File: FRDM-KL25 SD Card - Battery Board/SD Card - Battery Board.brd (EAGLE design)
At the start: 81.3 x 53.3 mm, 70 parts, among them J10 SSW-103-02-S-S, J11 SSW-102-02-S-S, J12 SSW-103-02-S-S, J13 SSW-103-02-S-S, J14 SSW-103-02-S-S, J15 SSW-103-02-S-S, J16 SSW-103-02-S-S, J17 SSW-103-02-S-S, J18 SSW-103-02-S-S, J19 501568-0207-V2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

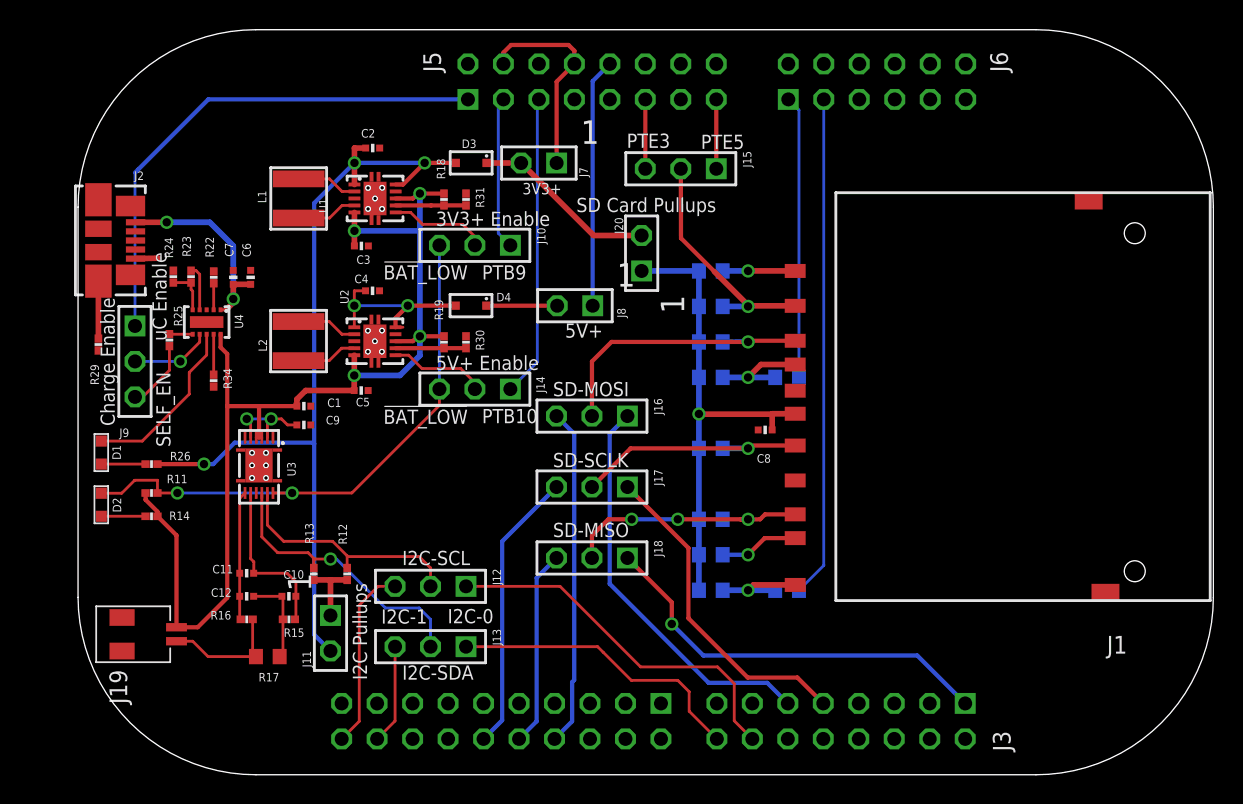
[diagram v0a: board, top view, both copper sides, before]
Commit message: FRDM-KL25Z-I: Some routing have been slighty shifted to give a cleaner look and better electrical flow
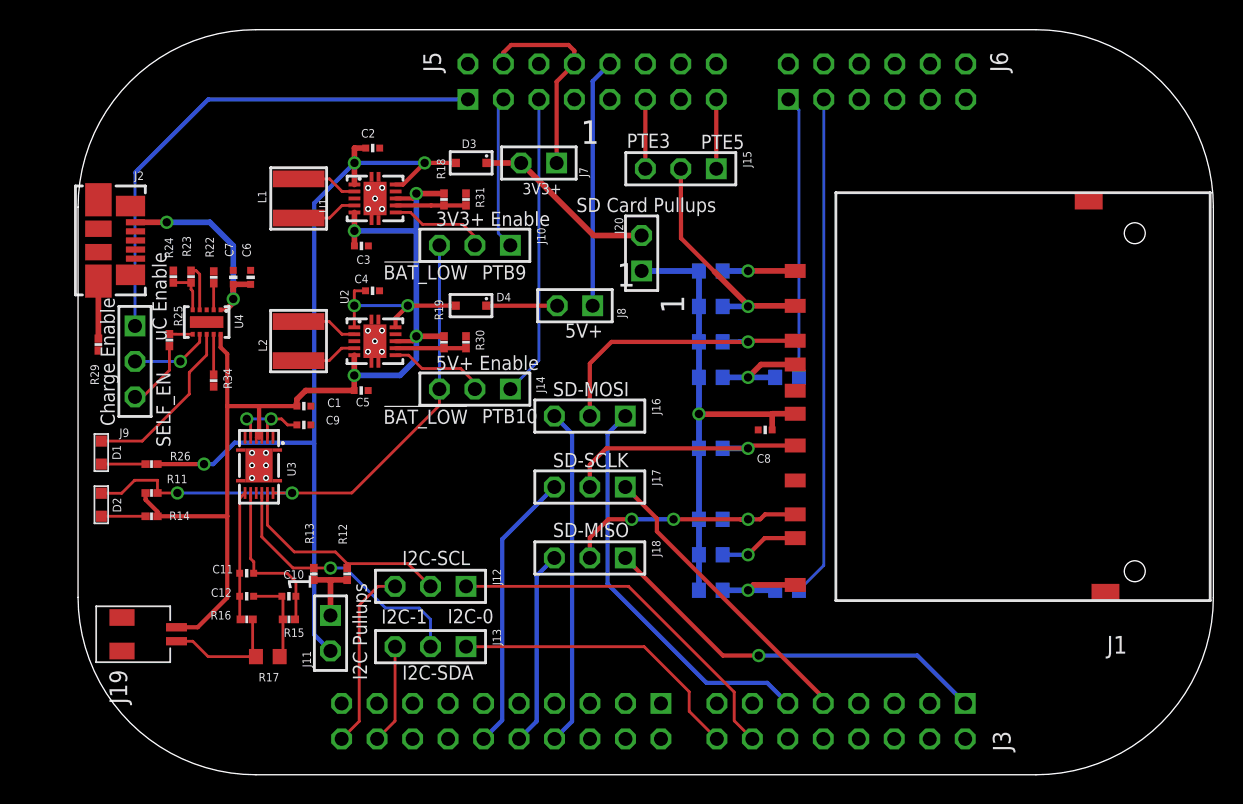
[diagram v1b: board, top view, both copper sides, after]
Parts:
- moved J16 0.15 mm to (21.7, 22.9)
- moved J17 0.15 mm to (21.7, 17.8)
- moved J18 0.15 mm to (21.7, 12.7)
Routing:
- net PACK+: track 80.3 -> 76.6 mm
- net SPI-SCLK-SD-B: track 23.4 -> 21.4 mm
- net GND: track 8.15 -> 6.51 mm
- net SCL: track 17.4 -> 16.1 mm
- net N$30: track 17.6 -> 18.7 mm
- net SPI-MISO-SD-B: track 29.4 -> 28.6 mm
- net SDA: track 20.3 -> 19.6 mm
- net N$20: track 13.1 -> 12.6 mm

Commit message: FRDM-KL25Z-I: Fixing a critical issue with power to the SD Card, when pullups are disabled so was the SD Card this has been partialy fixed but there is still a missing link from 3V3-SD to the SD Card. Also in need is the purpetual power to the Card Detect and Write Protect pins, this also needs to be connected to 3V3-SD
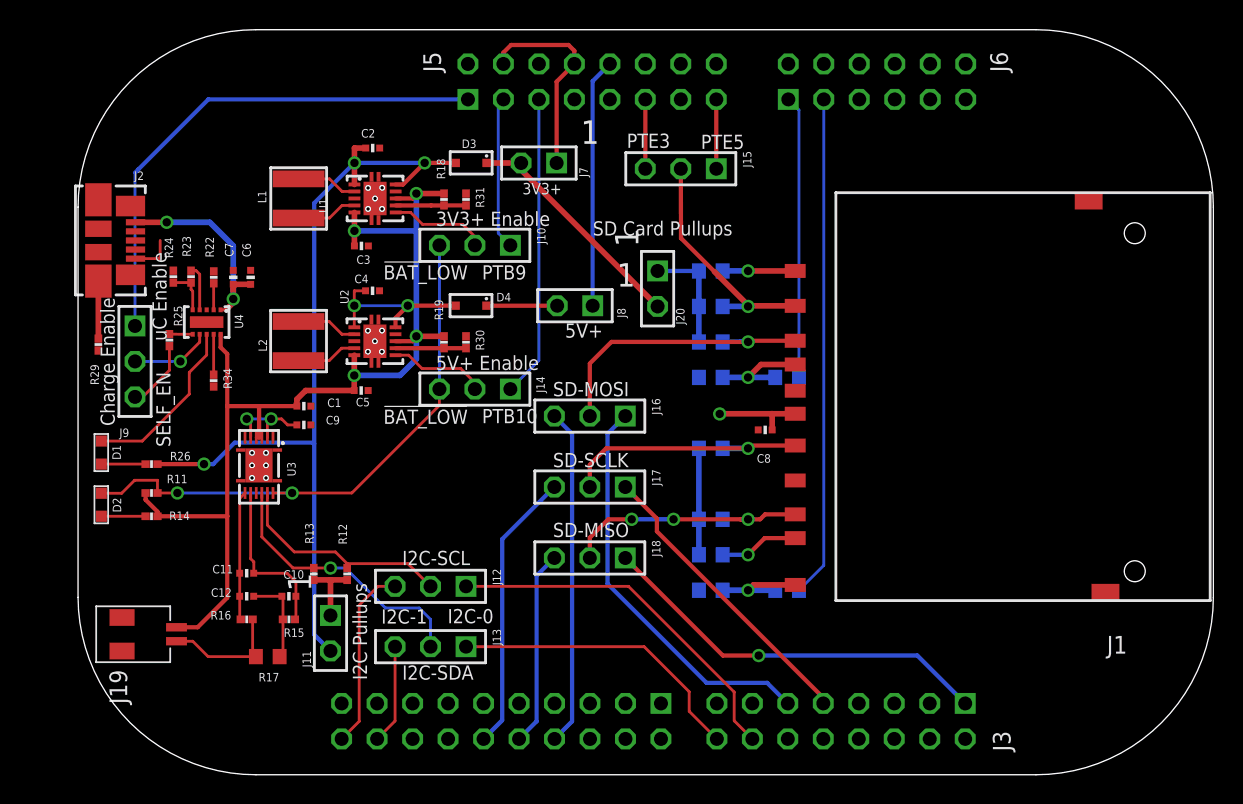
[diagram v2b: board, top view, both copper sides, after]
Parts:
- moved J20 2.79 mm to (26.5, 32.0), turned to 270 degrees
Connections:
- removed net N$17: D3.P$1, J20.2, J7.2
- new net +3V3-SD-PULLUP: J20.1, R1.2, R2.2, R3.2, R4.2, R5.2, R6.2
- net +3V3-SD: now also D3.P$1, J20.2, J7.2; no longer J20.1, R1.2, R2.2, R3.2, R4.2, R5.2, R6.2
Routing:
- net +3V3-SD-PULLUP: track 0.00 -> 15.7 mm
- net N$17: track 13.3 -> 0.00 mm
- net +3V3-SD: track 35.1 -> 23.3 mm
- net GND: track 6.51 -> 9.57 mm
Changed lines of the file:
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@@
 <text x="16.8656" y="38.735" size="0.8128" layer="21" ratio="5">3V3+</text>
 <text x="19.9136" y="28.4734" size="1.016" layer="21" ratio="5">5V+</text>
-<text x="20.7264" y="37.465" size="1.016" layer="21" ratio="5">SD Card Pullups</text>
+<text x="21.8948" y="35.7886" size="1.016" layer="21" ratio="5">SD Card Pullups</text>
 <text x="29.6418" y="41.9862" size="1.016" layer="21" ratio="5">PTE5</text>
 <text x="24.3332" y="42.0624" size="1.016" layer="21" ratio="5">PTE3</text>
@@
 <attribute name="VALUE" x="-13.97" y="4.699" size="1.27" layer="27" rot="R270"/>
 </element>
-<element name="J20" library="Kas-Connectors" package="SSW-102-02-S-S" value="SSW-102-02-S-S" x="25.4" y="34.5186" smashed="yes" rot="R90">
-<attribute name="OC_NEWARK" value="11P9351" x="25.4" y="34.5186" size="1.778" layer="27" rot="R90" display="off"/>
-<attribute name="MPN" value="SSW-102-02-S-S" x="25.4" y="34.5186" size="1.778" layer="27" rot="R90" display="off"/>
-<attribute name="MF" value="" x="25.4" y="34.5186" size="1.778" layer="27" rot="R90" display="off"/>
-<attribute name="OC_FARNELL" value="unknown" x="25.4" y="34.5186" size="1.778" layer="27" rot="R90" display="off"/>
-<attribute name="NAME" x="23.4696" y="37.084" size="0.6096" layer="25" rot="R270"/>
-<attribute name="VALUE" x="26.67" y="38.9636" size="1.27" layer="27" rot="R180"/>
+<element name="J20" library="Kas-Connectors" package="SSW-102-02-S-S" value="SSW-102-02-S-S" x="26.543" y="31.9786" smashed="yes" rot="R270">
+<attribute name="OC_NEWARK" value="11P9351" x="26.543" y="31.9786" size="1.778" layer="27" rot="R270" display="off"/>
+<attribute name="MPN" value="SSW-102-02-S-S" x="26.543" y="31.9786" size="1.778" layer="27" rot="R270" display="off"/>
+<attribute name="MF" value="" x="26.543" y="31.9786" size="1.778" layer="27" rot="R270" display="off"/>
+<attribute name="OC_FARNELL" value="unknown" x="26.543" y="31.9786" size="1.778" layer="27" rot="R270" display="off"/>
+<attribute name="NAME" x="28.4734" y="29.4132" size="0.6096" layer="25" rot="R90"/>
+<attribute name="VALUE" x="25.273" y="27.5336" size="1.27" layer="27"/>
 </element>
 </elements>
 <signals>
-<signal name="GND">
+<signal name="GND" airwireshidden="yes">
 <contactref element="U3" pad="P$1"/>
 <contactref element="U3" pad="P$6"/>
@@
 <wire x1="-0.27768125" y1="8.3058" x2="-0.27768125" y2="5.8751" width="0.2032" layer="1"/>
 <wire x1="-0.27768125" y1="5.8751" x2="-0.51398125" y2="5.6388" width="0.2032" layer="1"/>
+<wire x1="-10.8331" y1="34.133" x2="-9.0678" y2="34.133" width="0.2032" layer="1"/>
+<wire x1="-9.0678" y1="34.133" x2="-9.0678" y2="35.433" width="0.2032" layer="1"/>
 <wire x1="25.66543125" y1="48.071278125" x2="28.20543125" y2="48.071278125" width="0" layer="19" extent="1-1"/>
 <wire x1="12.827" y1="38.79121875" x2="25.66543125" y2="48.071278125" width="0" layer="19" extent="1-1"/>
@@
 <wire x1="-2.5908" y1="33.2914" x2="-3.8354" y2="33.2914" width="0" layer="19" extent="1-1"/>
 <wire x1="-8.128" y1="33.2672" x2="-5.2324" y2="33.2164" width="0" layer="19" extent="1-1"/>
-<wire x1="-10.8331" y1="34.133" x2="-8.128" y2="33.2672" width="0" layer="19" extent="1-1"/>
+<wire x1="-9.0678" y1="34.133" x2="-8.128" y2="33.2672" width="0" layer="19" extent="1-1"/>
 <wire x1="12.827" y1="28.5708" x2="7.7802" y2="28.7186" width="0" layer="19" extent="1-1"/>
 <wire x1="-13.4931" y1="27.5562" x2="-10.8331" y2="34.133" width="0" layer="19" extent="1-1"/>
@@
 <contactref element="J1" pad="P$4"/>
 <contactref element="C8" pad="1"/>
+<wire x1="36.396" y1="23.0256" x2="34.746" y2="23.0256" width="0.4064" layer="1"/>
+<wire x1="34.746" y1="21.8692" x2="34.746" y2="23.0256" width="0.4064" layer="1"/>
+<via x="30.988" y="23.0124" extent="1-16" drill="0.6"/>
+<contactref element="D3" pad="P$1"/>
+<contactref element="J7" pad="2"/>
+<contactref element="J20" pad="2"/>
+<wire x1="14.294759375" y1="40.985109375" x2="14.30205" y2="40.97781875" width="0.2032" layer="1"/>
+<wire x1="14.30205" y1="40.97781875" x2="16.774159375" y2="40.97781875" width="0.4064" layer="1"/>
+<wire x1="26.543" y1="30.7086" x2="16.774159375" y2="40.477440625" width="0.4064" layer="1"/>
+<wire x1="16.774159375" y1="40.477440625" x2="16.774159375" y2="40.97781875" width="0.4064" layer="1"/>
+<wire x1="31.0012" y1="23.0256" x2="34.746" y2="23.0256" width="0.4064" layer="1"/>
+<contactref element="R7" pad="2"/>
+<contactref element="R8" pad="2"/>
+<wire x1="31.0012" y1="23.0256" x2="30.988" y2="23.0124" width="0" layer="19" extent="1-1"/>
+<wire x1="29.503" y1="25.6286" x2="30.988" y2="23.0124" width="0" layer="19" extent="16-16"/>
+<wire x1="26.543" y1="30.7086" x2="29.503" y2="25.6286" width="0" layer="19" extent="16-16"/>
+<wire x1="29.503" y1="10.3886" x2="34.746" y2="21.8692" width="0" layer="19" extent="1-16"/>
+</signal>
+<signal name="+3V3-SD-PULLUP">
 <contactref element="R1" pad="2"/>
-<contactref element="R8" pad="2"/>
 <contactref element="R2" pad="2"/>
 <contactref element="R3" pad="2"/>
@@
 <contactref element="R5" pad="2"/>
 <contactref element="R6" pad="2"/>
-<contactref element="R7" pad="2"/>
 <wire x1="29.503" y1="28.1686" x2="29.503" y2="30.7086" width="0.4064" layer="16"/>
 <wire x1="29.503" y1="30.7086" x2="29.503" y2="33.2486" width="0.4064" layer="16"/>
 <wire x1="29.503" y1="20.5486" x2="29.503" y2="15.4686" width="0.4064" layer="16"/>
 <wire x1="29.503" y1="12.9286" x2="29.503" y2="15.4686" width="0.4064" layer="16"/>
-<wire x1="29.503" y1="12.9286" x2="29.503" y2="10.3886" width="0.4064" layer="16"/>
-<wire x1="36.396" y1="23.0256" x2="34.746" y2="23.0256" width="0.4064" layer="1"/>
-<wire x1="34.746" y1="21.8692" x2="34.746" y2="22.9948375" width="0.4064" layer="1"/>
 <contactref element="J20" pad="1"/>
-<wire x1="34.746" y1="22.9948375" x2="34.746" y2="23.0256" width="0.4064" layer="1"/>
-<wire x1="34.746" y1="22.9948375" x2="29.4561625" y2="22.9948375" width="0.4064" layer="1"/>
-<wire x1="29.4561625" y1="22.9948375" x2="29.503" y2="23.0124" width="0.4064" layer="1"/>
-<via x="29.503" y="23.0124" extent="1-16" drill="0.6"/>
-<wire x1="29.503" y1="23.0124" x2="29.503" y2="28.1686" width="0.4064" layer="16"/>
-<wire x1="29.503" y1="20.5486" x2="29.503" y2="23.0124" width="0.4064" layer="16"/>
-<wire x1="25.4" y1="33.2486" x2="29.503" y2="33.2486" width="0.4064" layer="16"/>
-<wire x1="29.503" y1="28.1686" x2="29.503" y2="25.6286" width="0" layer="19" extent="16-16"/>
-</signal>
-<signal name="N$17">
-<contactref element="D3" pad="P$1"/>
-<contactref element="J7" pad="2"/>
-<contactref element="J20" pad="2"/>
-<wire x1="14.294759375" y1="40.985109375" x2="14.30205" y2="40.97781875" width="0.2032" layer="1"/>
-<wire x1="14.30205" y1="40.97781875" x2="16.774159375" y2="40.97781875" width="0.4064" layer="1"/>
-<wire x1="16.774159375" y1="40.97781875" x2="21.963378125" y2="35.7886" width="0.4064" layer="1"/>
-<wire x1="21.963378125" y1="35.7886" x2="25.4" y2="35.7886" width="0.4064" layer="1"/>
+<wire x1="26.543" y1="33.2486" x2="29.503" y2="33.2486" width="0.3048" layer="16"/>
+<wire x1="29.503" y1="20.5486" x2="29.503" y2="28.1686" width="0" layer="19" extent="16-16"/>
 </signal>
 </signals>

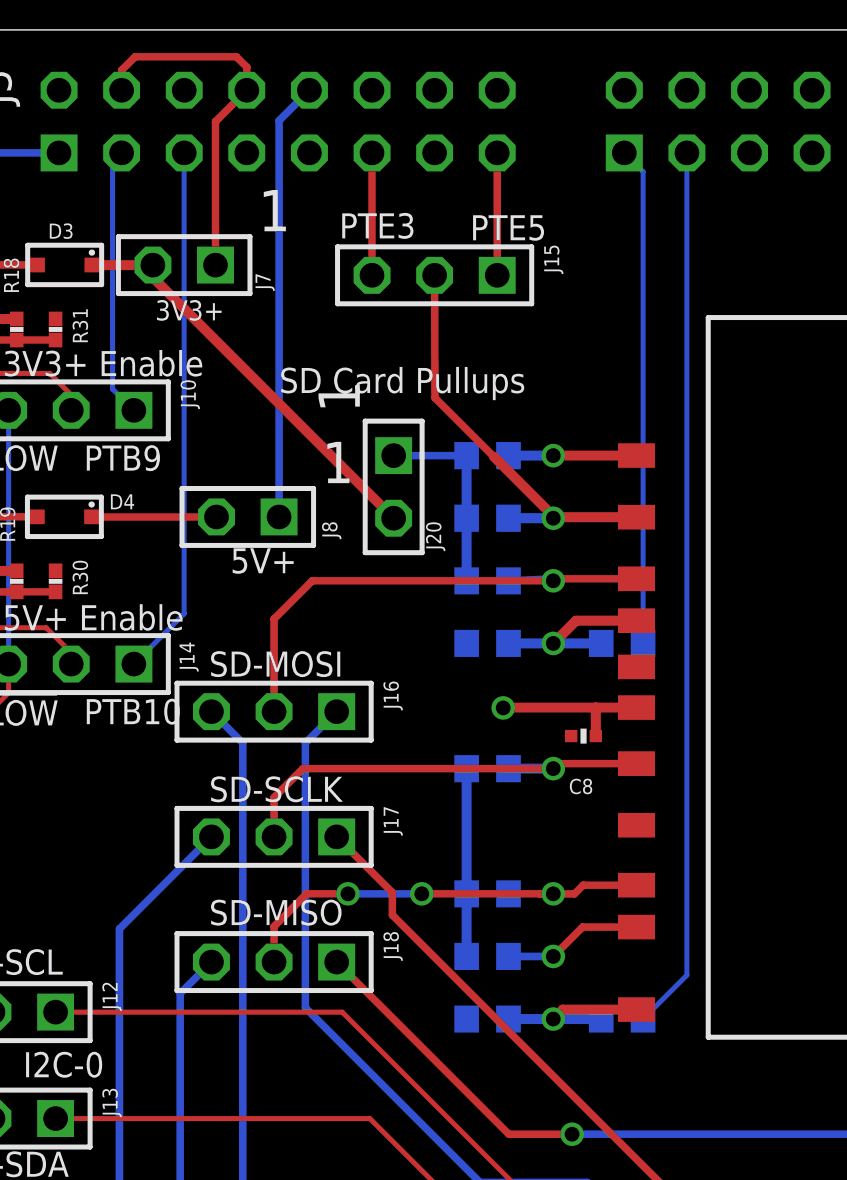
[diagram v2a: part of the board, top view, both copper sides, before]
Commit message: FRDM-KL25Z-I: SD Card power issue is resolved, connections have been rerouted to allow for the SD Card to always be powerd as well for the card detect and write protect to be always powerd.
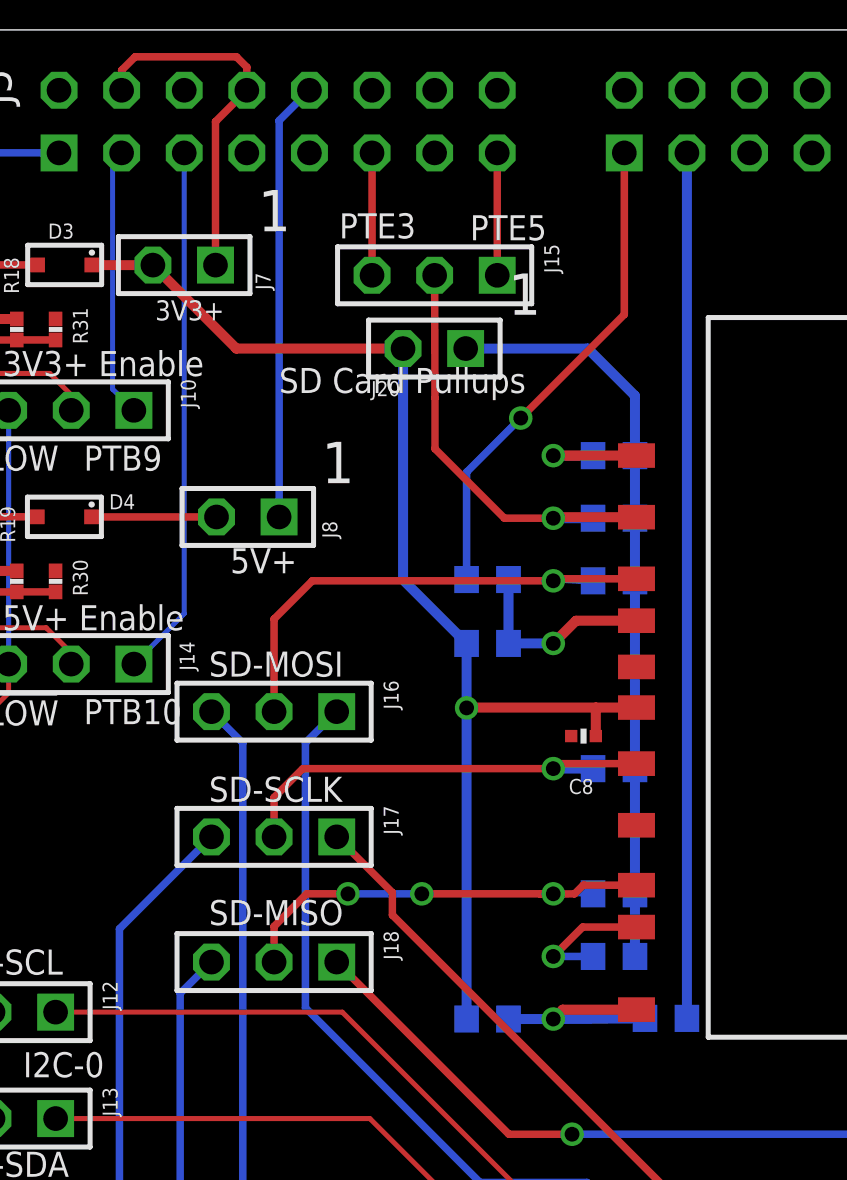
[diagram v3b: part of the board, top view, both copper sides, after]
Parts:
- moved R9 6.04 mm to (30.4, 28.2), turned to 180 degrees
- moved J20 5.85 mm to (28.2, 37.6), turned to 180 degrees
- moved R1 5.13 mm to (35.5, 33.2), turned to 180 degrees
- moved R2 5.13 mm to (35.5, 30.7), turned to 180 degrees
- moved R3 5.13 mm to (35.5, 28.2), turned to 180 degrees
- moved R4 5.13 mm to (35.5, 20.5), turned to 180 degrees
- moved R5 5.13 mm to (35.5, 15.5), turned to 180 degrees
- moved R6 5.13 mm to (35.5, 12.9), turned to 180 degrees
- moved R10 1.78 mm to (37.6, 10.4)
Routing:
- net +3V3-SD: track 23.3 -> 50.4 mm
- net +3V3-SD-PULLUP: track 15.7 -> 30.4 mm
- net N$26: track 7.30 -> 9.07 mm
- net N$23: track 17.0 -> 18.0 mm
- net SD-WRITE-PROTECT: track 35.9 -> 35.1 mm
- net N$19: track 7.52 -> 8.17 mm
- net SD-CARD-DETECT: track 20.2 -> 20.0 mm, vias 0 -> 1
